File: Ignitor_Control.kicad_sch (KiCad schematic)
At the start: 18 parts, among them J20 Ignitor Screw Terminal, K2 G5Q-1A DC24, Q8 BSS138, U8 INA199A2DCK

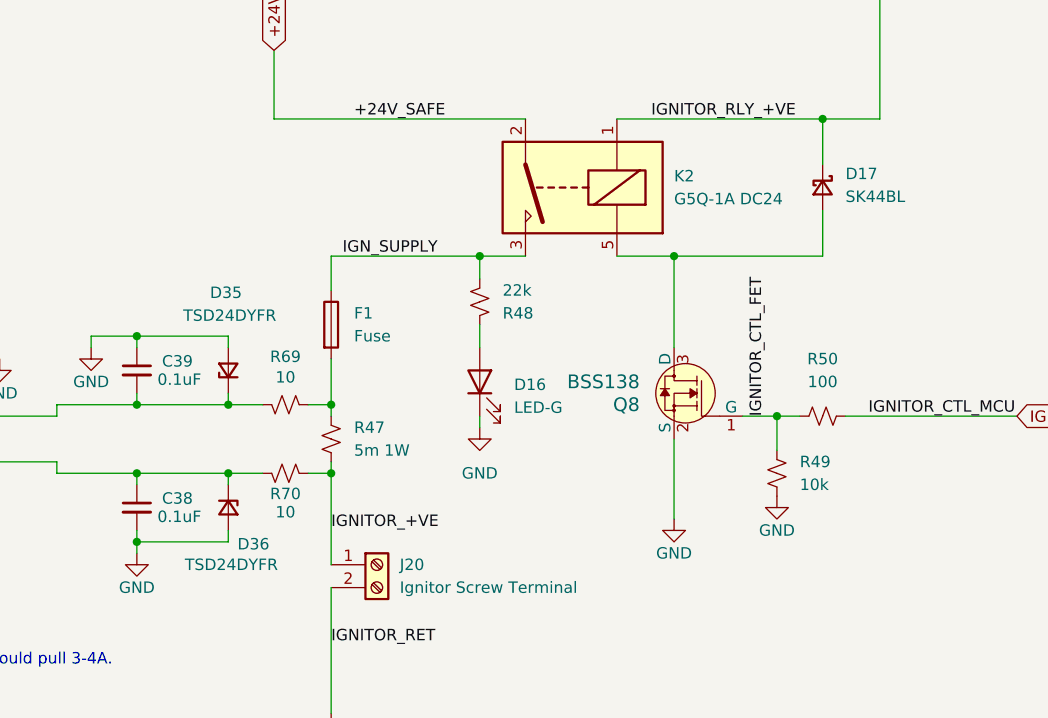
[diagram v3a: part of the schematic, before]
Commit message: pcb first draft, changed esp32 pin connections
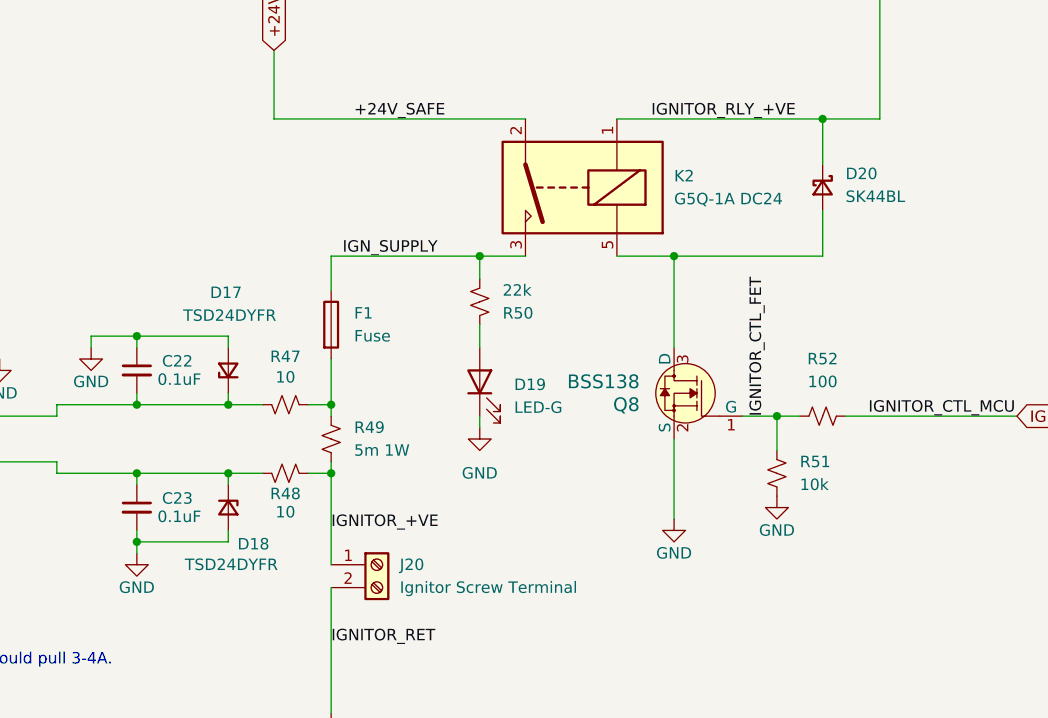
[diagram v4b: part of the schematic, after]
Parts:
- C22: renamed from C39; footprint (none) -> Capacitor_SMD:C_0603_1608Metric
- C23: renamed from C38; footprint (none) -> Capacitor_SMD:C_0603_1608Metric
- D17: renamed from D35; footprint (none) -> Diode_SMD:D_SOD-323
- D18: renamed from D36; footprint (none) -> Diode_SMD:D_SOD-323
- renumbered D16 to D19, D17 to D20, R69 to R47, R70 to R48, R47 to R49, R48 to R50, R49 to R51, R50 to R52
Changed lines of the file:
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@@
 		(dnp no)
 		(fields_autoplaced yes)
-		(property "Reference" "D16"
+		(property "Reference" "D19"
 			(at 182.88 103.1874 90)
 			(effects
@@
 			(project "panda"
 				(path "/226c5870-4123-4efa-a2b3-b42d02f59bb7/4e09186f-4067-4c22-bbd5-0048a728fd95"
-					(reference "D16")
+					(reference "D19")
 					(unit 1)
 				)
@@
 		(dnp no)
 		(fields_autoplaced yes)
-		(property "Reference" "#PWR0114"
+		(property "Reference" "#PWR0115"
 			(at 116.84 100.33 0)
 			(effects
@@
 			(project "panda"
 				(path "/226c5870-4123-4efa-a2b3-b42d02f59bb7/4e09186f-4067-4c22-bbd5-0048a728fd95"
-					(reference "#PWR0114")
+					(reference "#PWR0115")
 					(unit 1)
 				)
@@
 		(dnp no)
 		(fields_autoplaced yes)
-		(property "Reference" "R47"
+		(property "Reference" "R49"
 			(at 165.1 107.9499 0)
 			(effects
@@
 			(project ""
 				(path "/226c5870-4123-4efa-a2b3-b42d02f59bb7/4e09186f-4067-4c22-bbd5-0048a728fd95"
-					(reference "R47")
+					(reference "R49")
 					(unit 1)
 				)
@@
 		(dnp no)
 		(fields_autoplaced yes)
-		(property "Reference" "#PWR0118"
+		(property "Reference" "#PWR0121"
 			(at 179.07 114.3 0)
 			(effects
@@
 			(project "panda"
 				(path "/226c5870-4123-4efa-a2b3-b42d02f59bb7/4e09186f-4067-4c22-bbd5-0048a728fd95"
-					(reference "#PWR0118")
+					(reference "#PWR0121")
 					(unit 1)
 				)
@@
 		(on_board yes)
 		(dnp no)
-		(property "Reference" "#PWR0115"
+		(property "Reference" "#PWR0116"
 			(at 116.84 127 0)
 			(effects
@@
 			(project "panda"
 				(path "/226c5870-4123-4efa-a2b3-b42d02f59bb7/4e09186f-4067-4c22-bbd5-0048a728fd95"
-					(reference "#PWR0115")
+					(reference "#PWR0116")
 					(unit 1)
 				)
@@
 		(on_board yes)
 		(dnp no)
-		(property "Reference" "C38"
+		(property "Reference" "C23"
 			(at 143.764 115.824 0)
 			(effects
@@
 			)
 		)
-		(property "Footprint" ""
+		(property "Footprint" "Capacitor_SMD:C_0603_1608Metric"
 			(at 140.97 116.84 0)
 			(effects
@@
 			(project ""
 				(path "/226c5870-4123-4efa-a2b3-b42d02f59bb7/4e09186f-4067-4c22-bbd5-0048a728fd95"
-					(reference "C38")
+					(reference "C23")
 					(unit 1)
 				)
@@
 		(on_board yes)
 		(dnp no)
-		(property "Reference" "#PWR0117"
+		(property "Reference" "#PWR0120"
 			(at 162.56 146.05 0)
 			(effects
@@
 			(project "nexus"
 				(path "/226c5870-4123-4efa-a2b3-b42d02f59bb7/4e09186f-4067-4c22-bbd5-0048a728fd95"
-					(reference "#PWR0117")
+					(reference "#PWR0120")
 					(unit 1)
 				)
@@
 		(on_board yes)
 		(dnp no)
-		(property "Reference" "D35"
+		(property "Reference" "D17"
 			(at 152.654 92.964 90)
 			(effects
@@
 			)
 		)
-		(property "Footprint" ""
+		(property "Footprint" "Diode_SMD:D_SOD-323"
 			(at 151.13 101.6 90)
 			(effects
@@
 			(project ""
 				(path "/226c5870-4123-4efa-a2b3-b42d02f59bb7/4e09186f-4067-4c22-bbd5-0048a728fd95"
-					(reference "D35")
+					(reference "D17")
 					(unit 1)
 				)
@@
 		(on_board yes)
 		(dnp no)
-		(property "Reference" "#PWR0119"
+		(property "Reference" "#PWR0122"
 			(at 200.66 124.46 0)
 			(effects
@@
 			(project "nexus"
 				(path "/226c5870-4123-4efa-a2b3-b42d02f59bb7/4e09186f-4067-4c22-bbd5-0048a728fd95"
-					(reference "#PWR0119")
+					(reference "#PWR0122")
 					(unit 1)
 				)
@@
 		(on_board yes)
 		(dnp no)
-		(property "Reference" "#PWR0157"
+		(property "Reference" "#PWR0118"
 			(at 135.89 105.41 0)
 			(effects
@@
 			(project "panda"
 				(path "/226c5870-4123-4efa-a2b3-b42d02f59bb7/4e09186f-4067-4c22-bbd5-0048a728fd95"
-					(reference "#PWR0157")
+					(reference "#PWR0118")
 					(unit 1)
 				)
@@
 		(dnp no)
 		(fields_autoplaced yes)
-		(property "Reference" "R49"
+		(property "Reference" "R51"
 			(at 214.63 111.7599 0)
 			(effects
@@
 			(project "panda"
 				(path "/226c5870-4123-4efa-a2b3-b42d02f59bb7/4e09186f-4067-4c22-bbd5-0048a728fd95"
-					(reference "R49")
+					(reference "R51")
 					(unit 1)
 				)
@@
 		(dnp no)
 		(fields_autoplaced yes)
-		(property "Reference" "D17"
+		(property "Reference" "D20"
 			(at 219.71 79.7559 90)
 			(effects
@@
 			(project "nexus"
 				(path "/226c5870-4123-4efa-a2b3-b42d02f59bb7/4e09186f-4067-4c22-bbd5-0048a728fd95"
-					(reference "D17")
+					(reference "D20")
 					(unit 1)
 				)
@@
 		(on_board yes)
 		(dnp no)
-		(property "Reference" "#PWR0116"
+		(property "Reference" "#PWR0117"
 			(at 125.73 106.68 0)
 			(effects
@@
 			(project "panda"
 				(path "/226c5870-4123-4efa-a2b3-b42d02f59bb7/4e09186f-4067-4c22-bbd5-0048a728fd95"
-					(reference "#PWR0116")
+					(reference "#PWR0117")
 					(unit 1)
 				)
@@
 		(on_board yes)
 		(dnp no)
-		(property "Reference" "C39"
+		(property "Reference" "C22"
 			(at 143.764 100.584 0)
 			(effects
@@
 			)
 		)
-		(property "Footprint" ""
+		(property "Footprint" "Capacitor_SMD:C_0603_1608Metric"
 			(at 140.97 101.6 0)
 			(effects
@@
 			(project "panda"
 				(path "/226c5870-4123-4efa-a2b3-b42d02f59bb7/4e09186f-4067-4c22-bbd5-0048a728fd95"
-					(reference "C39")
+					(reference "C22")
 					(unit 1)
 				)
@@
 		(on_board yes)
 		(dnp no)
-		(property "Reference" "D36"
+		(property "Reference" "D18"
 			(at 152.146 120.904 90)
 			(effects
@@
 			)
 		)
-		(property "Footprint" ""
+		(property "Footprint" "Diode_SMD:D_SOD-323"
 			(at 151.13 116.84 90)
 			(effects
@@
 			(project "panda"
 				(path "/226c5870-4123-4efa-a2b3-b42d02f59bb7/4e09186f-4067-4c22-bbd5-0048a728fd95"
-					(reference "D36")
+					(reference "D18")
 					(unit 1)
 				)
@@
 		(on_board yes)
 		(dnp no)
-		(property "Reference" "#PWR0156"
+		(property "Reference" "#PWR0119"
 			(at 140.97 128.27 0)
 			(effects
@@
 			(project "panda"
 				(path "/226c5870-4123-4efa-a2b3-b42d02f59bb7/4e09186f-4067-4c22-bbd5-0048a728fd95"
-					(reference "#PWR0156")
+					(reference "#PWR0119")
 					(unit 1)
 				)
@@
 		(on_board yes)
 		(dnp no)
-		(property "Reference" "#PWR0120"
+		(property "Reference" "#PWR0123"
 			(at 212.09 121.92 0)
 			(effects
@@
 			(project "panda"
 				(path "/226c5870-4123-4efa-a2b3-b42d02f59bb7/4e09186f-4067-4c22-bbd5-0048a728fd95"
-					(reference "#PWR0120")
+					(reference "#PWR0123")
 					(unit 1)
 				)
@@
 		(dnp no)
 		(fields_autoplaced yes)
-		(property "Reference" "R48"
+		(property "Reference" "R50"
 			(at 181.61 95.2501 0)
 			(effects
@@
 			(project "panda"
 				(path "/226c5870-4123-4efa-a2b3-b42d02f59bb7/4e09186f-4067-4c22-bbd5-0048a728fd95"
-					(reference "R48")
+					(reference "R50")
 					(unit 1)
 				)
@@
 		(on_board yes)
 		(dnp no)
-		(property "Reference" "R69"
+		(property "Reference" "R47"
 			(at 157.48 100.076 90)
 			(effects
@@
 			(project "panda"
 				(path "/226c5870-4123-4efa-a2b3-b42d02f59bb7/4e09186f-4067-4c22-bbd5-0048a728fd95"
-					(reference "R69")
+					(reference "R47")
 					(unit 1)
 				)
@@
 		(dnp no)
 		(fields_autoplaced yes)
-		(property "Reference" "R50"
+		(property "Reference" "R52"
 			(at 217.17 100.33 90)
 			(effects
@@
 			(project "panda"
 				(path "/226c5870-4123-4efa-a2b3-b42d02f59bb7/4e09186f-4067-4c22-bbd5-0048a728fd95"
-					(reference "R50")
+					(reference "R52")
 					(unit 1)
 				)
@@
 		(on_board yes)
 		(dnp no)
-		(property "Reference" "R70"
+		(property "Reference" "R48"
 			(at 157.48 115.316 90)
 			(effects
@@
 			(project "panda"
 				(path "/226c5870-4123-4efa-a2b3-b42d02f59bb7/4e09186f-4067-4c22-bbd5-0048a728fd95"
-					(reference "R70")
-					(unit 1)
-				)
+					(reference "R48")
+					(unit 1)
+				)

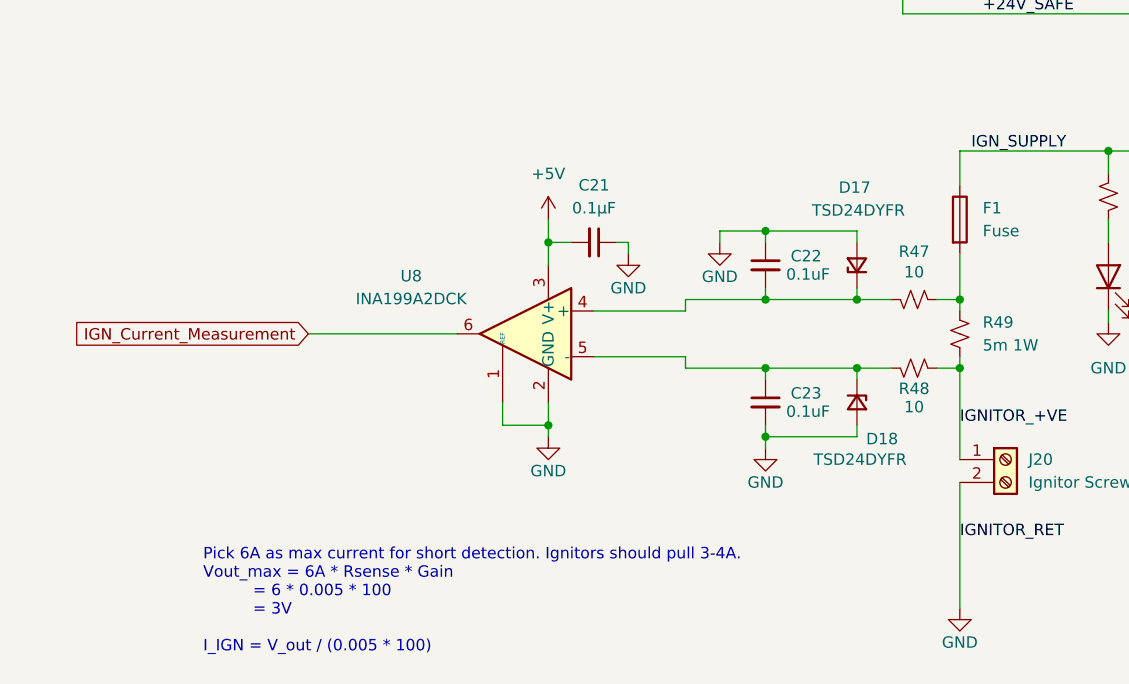
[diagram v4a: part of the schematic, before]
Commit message: replaced ignitor current sensor with INA187A3 for higher voltage tolerance
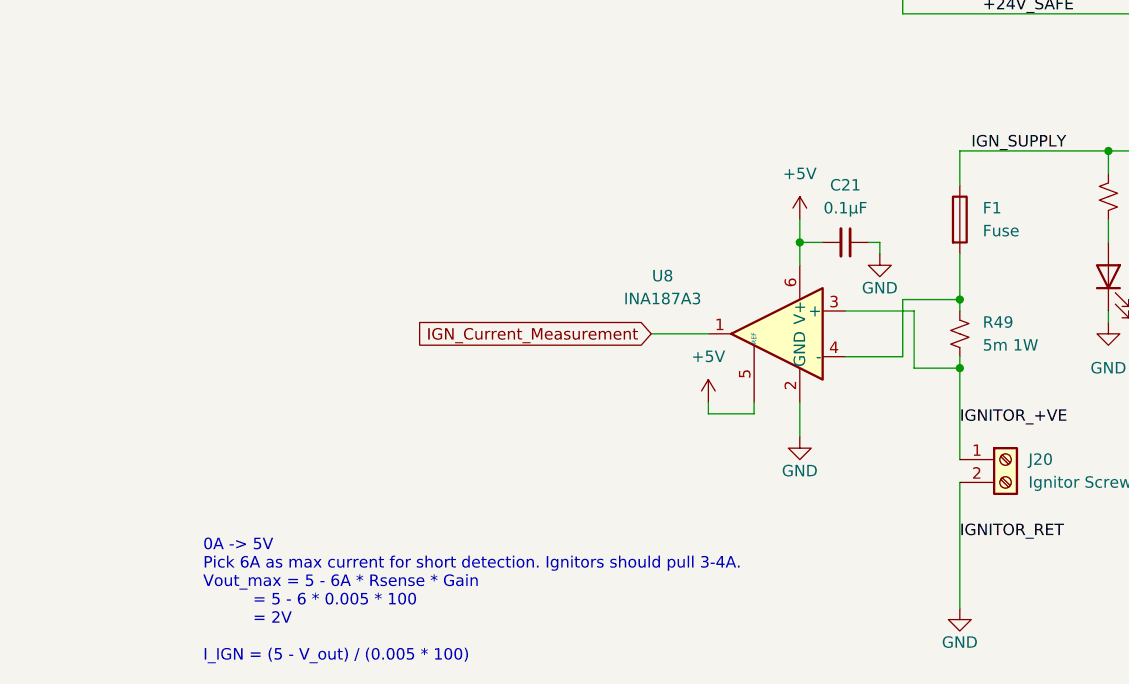
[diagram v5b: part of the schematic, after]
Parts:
- removed C22, C23: 0.1uF, Capacitor_SMD:C_0603_1608Metric, symbol Device:C_Small
- removed D17, D18: TSD24DYFR, Diode_SMD:D_SOD-323, symbol Device:D_Zener_Small
- removed R47, R48: 10, Resistor_SMD:R_0402_1005Metric, symbol Device:R_Small_US
- U8: value INA199A2DCK -> INA187A3; footprint Package_TO_SOT_SMD:SOT-363_SC-70-6 -> Package_TO_SOT_SMD:SOT-23-6
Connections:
- net +5V: now also U8.5 (REF), U8.6 (V+); no longer U8.3 (V+)
- net GND: no longer U8.1 (REF)
- net IGNITOR_+VE: now also U8.3 (+)
- net IGN_Current_Measurement: now also U8.1; no longer U8.6
- net at F1.2, R49.1: now also U8.4 (-)
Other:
- note added: "0A -> 5V Pick 6A as max current for short detection. Ignitors should pull 3-4A. Vout_max = 5 - 6A * Rsense * Gain = 5 - 6 * 0.005 * 100 = 2V I_IGN = (5 - V_out) / (0.005 * 100)"
- note removed: "Pick 6A as max current for short detection. Ignitors should pull 3-4A. Vout_max = 6A * Rsense * Gain = 6 * 0.005 * 100 = 3V I_IGN = V_out / (0.005 * 100)"
- moved on the sheet: C21, U8

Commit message: changed CSA to INA187A1 from INA187A3 for availability
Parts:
- R49: value 5m 1W -> 25m 1W
- U8: value INA187A3 -> INA187A1
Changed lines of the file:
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@@
 			)
 		)
-		(property "Value" "5m 1W"
+		(property "Value" "25m 1W"
 			(at 165.1 110.4899 0)
 			(effects
@@
 			)
 		)
-		(property "Value" "INA187A3"
+		(property "Value" "INA187A1"
 			(at 129.54 105.3398 0)
 			(effects
